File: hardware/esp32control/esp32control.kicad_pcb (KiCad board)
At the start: 2 copper layers, 67.6 x 85.9 mm, 86 parts, among them J1 Conn_02x10_Odd_Even, Q1 BSS138, Q2 BSS138, Q3 BSS138, Q4 BSS138, Q5 BSS138, Q6 BSS138, Q7 MMBT3904, Q8 MMBT3904, SW1 Boot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

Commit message: switched position of con and esp in layout
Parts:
- added REF**: OSHW-Logo2_7.3x6mm_SilkScreen, Symbol:OSHW-Logo2_7.3x6mm_SilkScreen, F.Cu at (84.9, 72.5)
- moved R33 37.5 mm to (83.3, 79.2), turned to 270 degrees
- moved D16 37.1 mm to (83.3, 82.6)
- moved J1 35.8 mm to (76.2, 66.1)
- moved R32 31.8 mm to (85.3, 79.2), turned to 270 degrees
- moved D15 31.7 mm to (85.3, 82.6)
- moved R20 31.6 mm to (107.7, 58.8), turned to 0 degrees
- moved Q8 25.9 mm to (107.5, 61.7), turned to 270 degrees
- moved U1 17.2 mm to (106.1, 76.6)
- moved R22 16.3 mm to (94.0, 88.8)
- moved R21 12.4 mm to (90.7, 90.5), turned to 180 degrees
- moved Q7 10.5 mm to (90.6, 87.8)
- moved TP1 1.17 mm to (70.7, 77.1)
- moved C5 0.42 mm to (66.2, 79.7)
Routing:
- net Net-(Q8-Pad1): track 2.14 -> 51.6 mm, vias 0 -> 2
- net Net-(Q7-Pad1): track 7.39 -> 51.6 mm, vias 0 -> 2
- net GND: track 203.7 -> 246.4 mm, vias 39 -> 55
- net /IO27: track 68.5 -> 36.8 mm, vias 4 -> 1
- net /OPTO3: track 9.40 -> 35.1 mm, vias 0 -> 2
- net /IO23: track 30.6 -> 52.6 mm
- net /OPTO4: track 8.74 -> 30.1 mm, vias 0 -> 2
- net /IO4: track 19.7 -> 39.8 mm
- net /SDA: track 92.4 -> 72.5 mm
- net +5V: track 121.7 -> 103.7 mm, vias 7 -> 6
- net /IO26: track 61.9 -> 44.6 mm, vias 4 -> 1
- net +3V3: track 183.8 -> 199.8 mm, vias 8 -> 7
- net /nBoot: track 92.1 -> 76.4 mm
- net /nReset: track 95.2 -> 81.7 mm, vias 7 -> 3
- net /RXD0: track 36.9 -> 47.6 mm, vias 1 -> 3
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
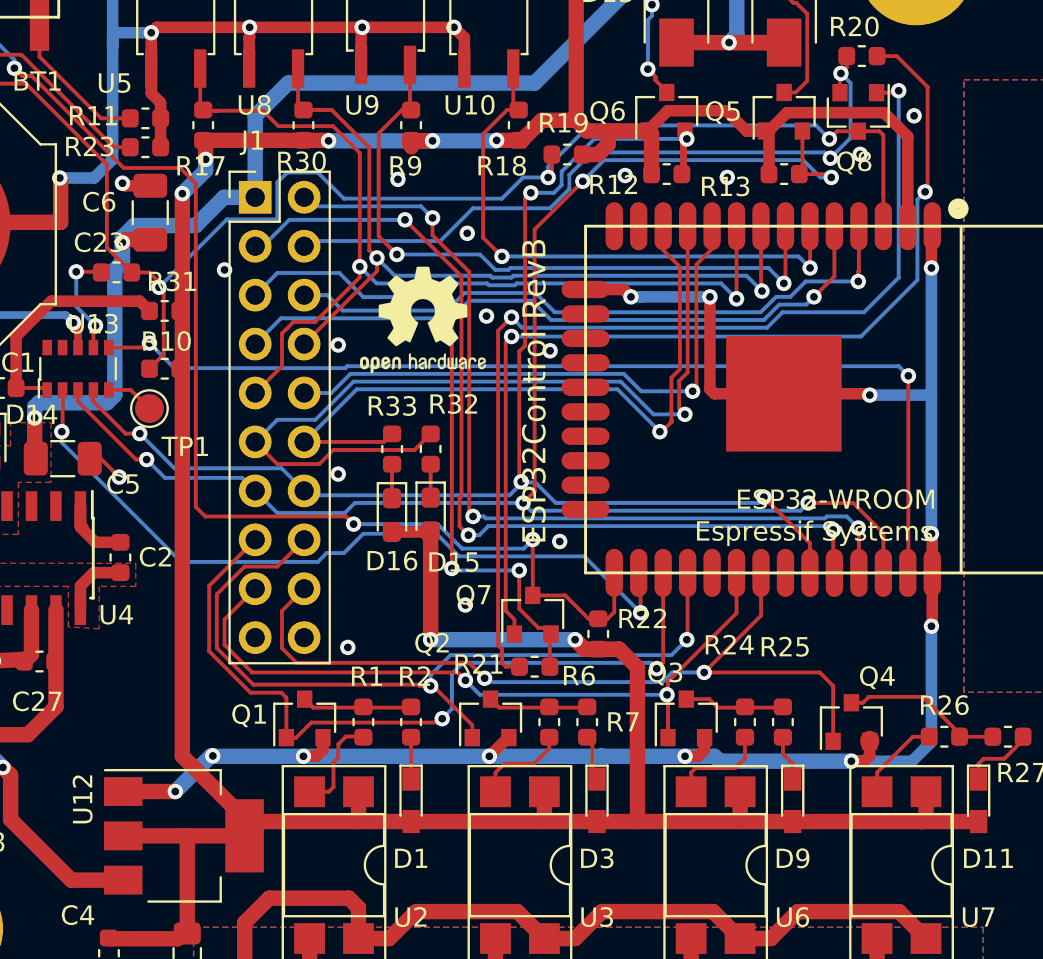
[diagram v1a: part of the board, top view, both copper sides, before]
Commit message: moved via out of pad
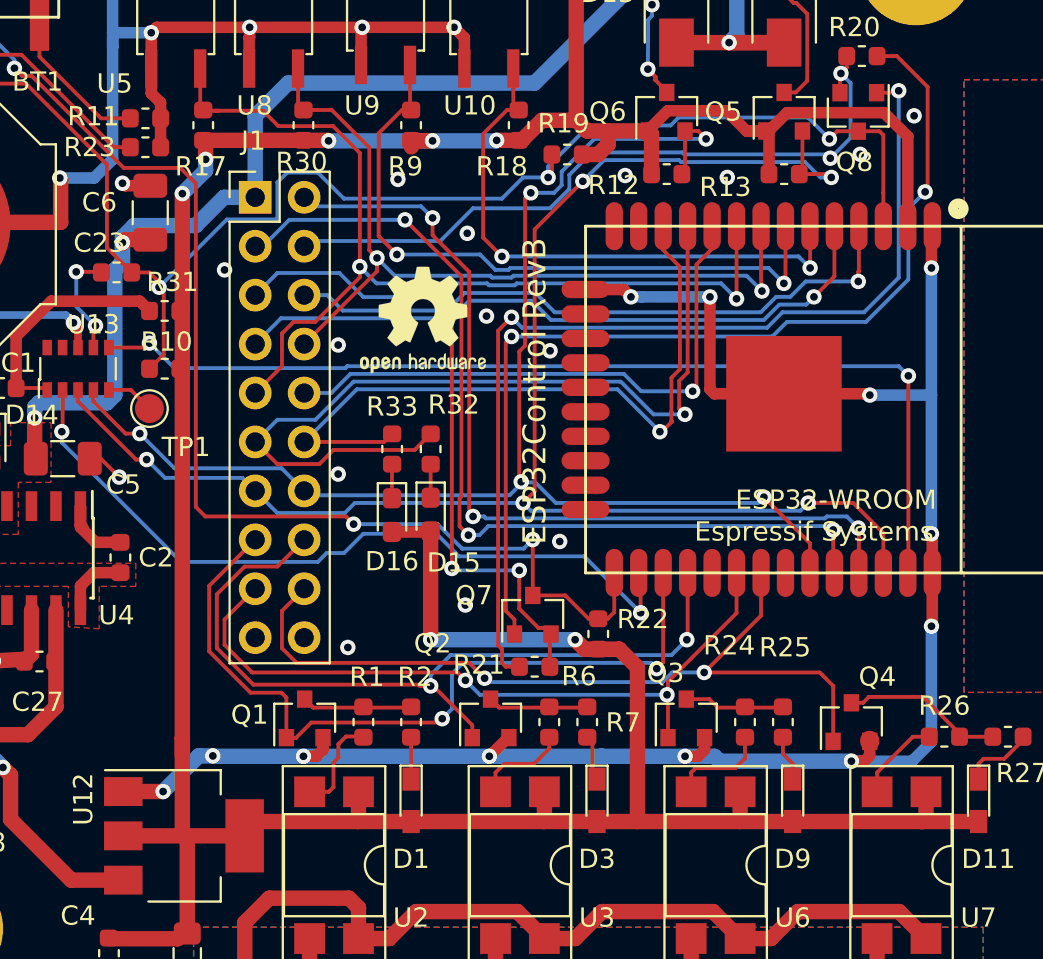
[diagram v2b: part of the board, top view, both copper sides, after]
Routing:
- net +3V3: track 199.8 -> 200.3 mm
